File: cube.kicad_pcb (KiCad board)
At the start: 2 copper layers, 300 parts, among them J1 serial_conn, J10 Conn_01x01, J11 Conn_01x01, J2 shifters_common_conn, J3 Conn_01x01, J4 Conn_01x01, J5 Conn_01x01, J6 Conn_01x01, J7 Conn_01x01, J8 Conn_01x01, J9 Conn_01x01, Q1 IRF9540N, Q2 IRF9540N, Q3 IRF9540N, Q4 IRF9540N, Q5 IRF9540N, Q6 IRF9540N, Q7 IRF9540N, Q8 IRF9540N, U1 SN74HC595N_0_b, U10 SN74HC595N_3_b, U11 SN74HC595N_3_g, U12 SN74HC595N_3_r, U13 SN74HC595N_4_b, U14 SN74HC595N_4_g, U15 SN74HC595N_4_r, U16 SN74HC595N_5_b, U17 SN74HC595N_5_g, U18 SN74HC595N_5_r, U19 SN74HC595N_6_b, U2 SN74HC595N_0_g, U20 SN74HC595N_6_g, U21 SN74HC595N_6_r, U22 SN74HC595N_7_b, U23 SN74HC595N_7_g, U24 SN74HC595N_7_r, U25 SN74HC595N_cols, U3 SN74HC595N_0_r, U4 SN74HC595N_1_b, U5 SN74HC595N_1_g, U6 SN74HC595N_1_r, U7 SN74HC595N_2_b, U8 SN74HC595N_2_g, U9 SN74HC595N_2_r

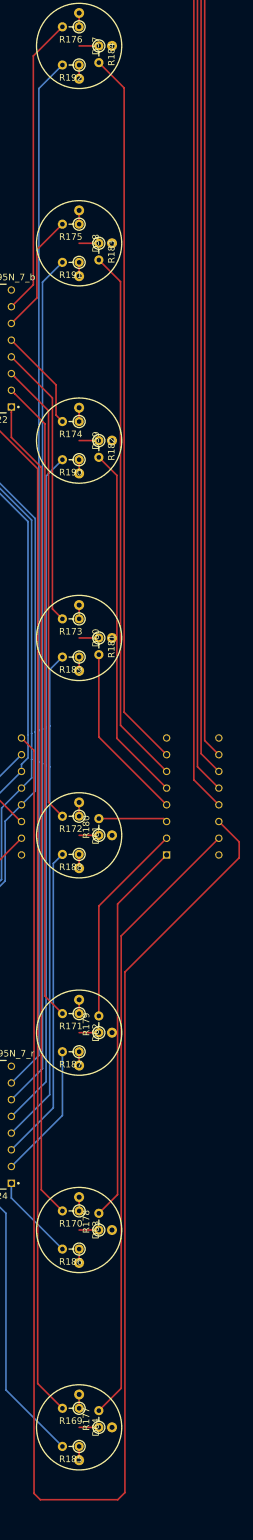
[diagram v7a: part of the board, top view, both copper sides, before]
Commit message: fix 8th rows's green conns
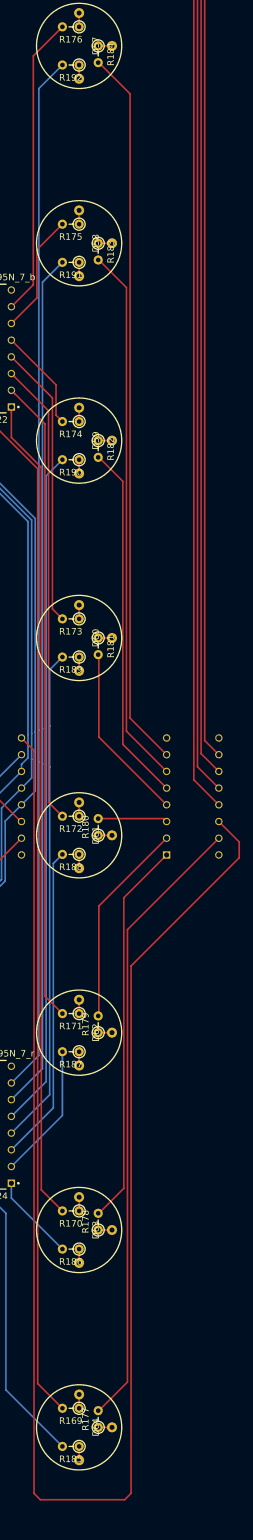
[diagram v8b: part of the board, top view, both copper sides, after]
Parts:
- moved R182 0.10 mm to (264.8, 150.0)
- moved R177 0.10 mm to (264.8, 300.0)
- moved R178 0.10 mm to (264.8, 270.0)
- moved R179 0.10 mm to (264.8, 240.0)
- moved R180 0.10 mm to (264.8, 210.0)
- moved R181 0.10 mm to (264.8, 180.0)
- moved R183 0.10 mm to (264.8, 120.0)
- moved R184 0.10 mm to (264.8, 90.0)
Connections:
- U19 pad 9: Net-(U19-Pad9) -> ser_out_6_b
- U20 pad 9: Net-(U20-Pad9) -> ser_out_6_g
- U21 pad 9: Net-(U21-Pad9) -> ser_out_6_r
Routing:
- net ser_out_6_g: track 0.00 -> 241.4 mm
- net ser_out_2_g: track 481.3 -> 240.5 mm
- net ser_out_2_r: track 326.9 -> 163.5 mm
- net ser_out_6_r: track 0.00 -> 163.4 mm
- net ser_out_6_b: track 0.00 -> 127.5 mm
- net ser_out_2_b: track 255.0 -> 127.5 mm
- net led_7_7_g: track 3.00 -> 2.10 mm
- net led_7_6_g: track 3.00 -> 2.10 mm
- net led_7_5_g: track 3.00 -> 2.10 mm
- net led_7_4_g: track 3.00 -> 2.10 mm
- net led_7_3_g: track 3.00 -> 2.10 mm
- net led_7_2_g: track 3.00 -> 2.10 mm
- net led_7_1_g: track 3.00 -> 2.10 mm
- net led_7_0_g: track 3.00 -> 2.10 mm
